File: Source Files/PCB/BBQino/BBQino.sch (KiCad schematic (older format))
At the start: 0 parts

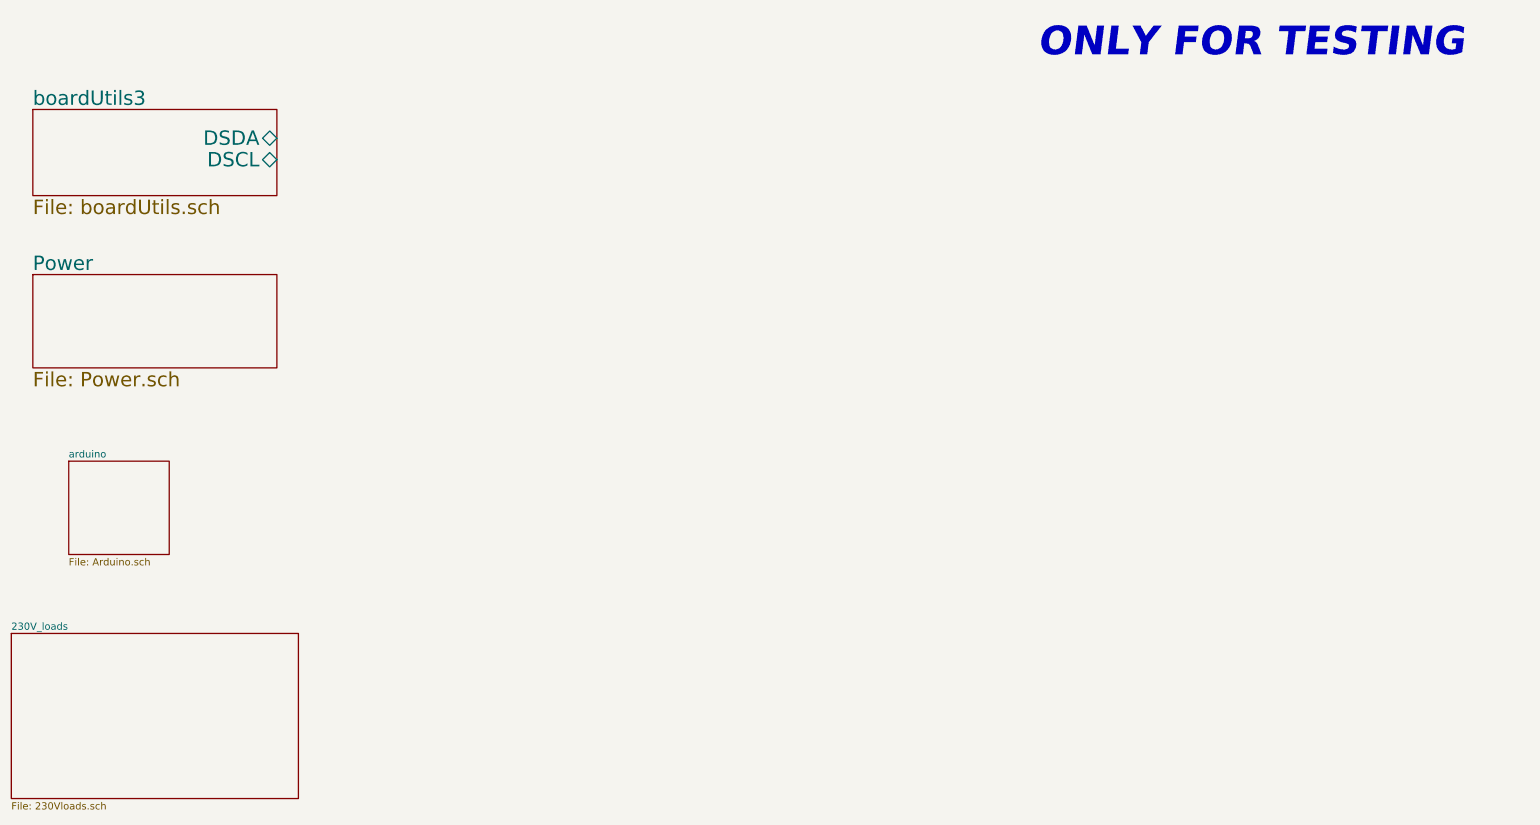
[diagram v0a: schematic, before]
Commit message: added thermocouple interface
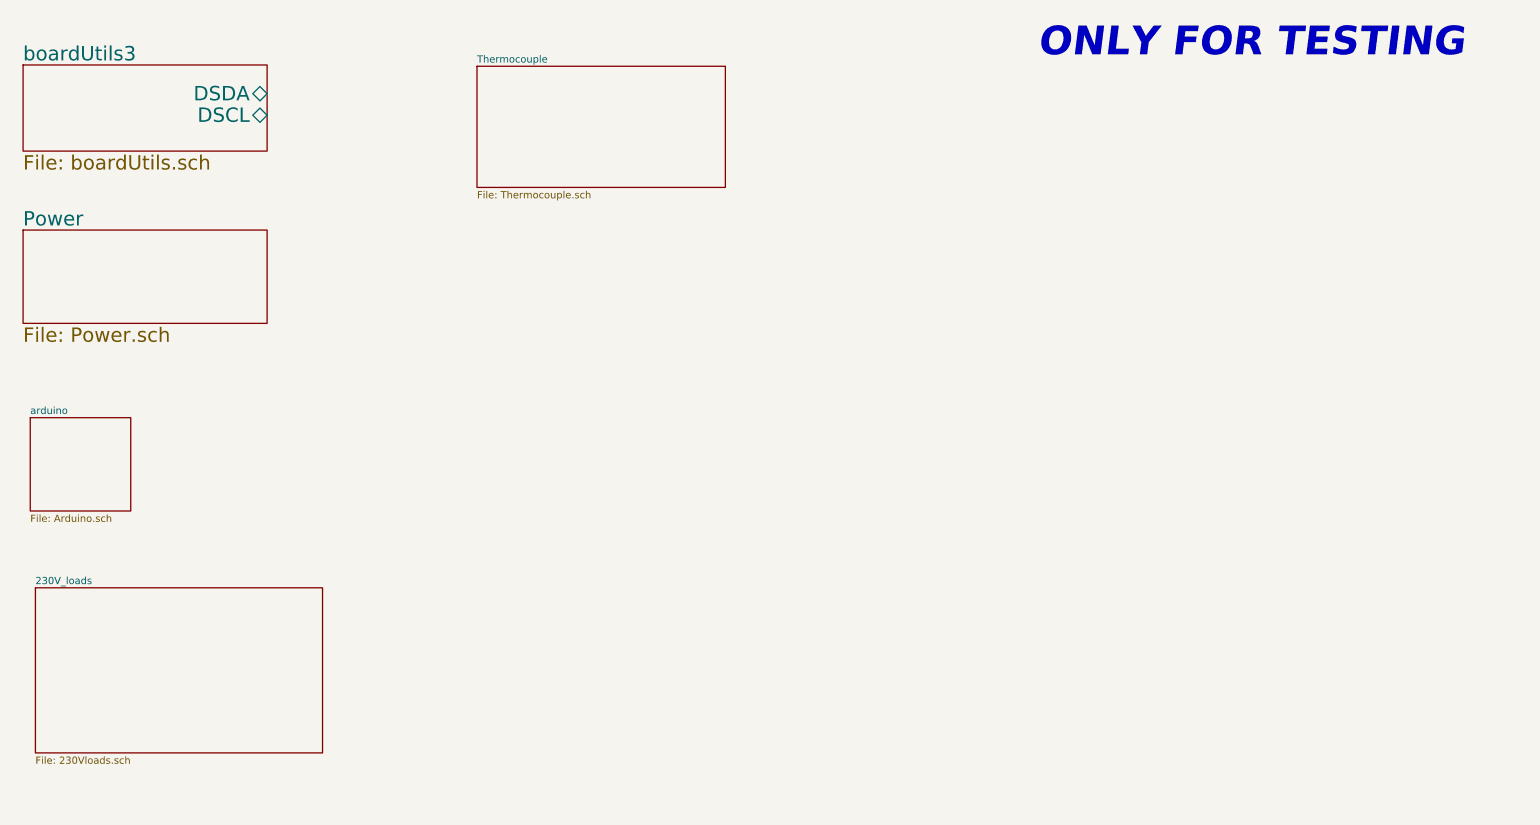
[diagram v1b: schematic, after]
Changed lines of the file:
@@
 $Descr A4 11693 8268
 encoding utf-8
-Sheet 1 5
+Sheet 1 6
 Title "BBQino - DRAFT"
 Date "2021-09-08"
@@
 ONLY FOR TESTING
 $Sheet
-S 1100 1350 1700 600
+S 1032 1040 1700 600
 U 61391ED2
 F0 "boardUtils3" 100
 F1 "boardUtils.sch" 100
-F2 "DSDA" B R 2800 1550 100
-F3 "DSCL" B R 2800 1700 100
+F2 "DSDA" B R 2732 1240 100
+F3 "DSCL" B R 2732 1390 100
 $EndSheet
 $Sheet
-S 1100 2500 1700 650
+S 1032 2190 1700 650
 U 613C1456
 F0 "Power" 100
@@
 $EndSheet
 $Sheet
-S 1350 3800 700  650
+S 1082 3497 700  650
 U 613FC6D4
 F0 "arduino" 50
@@
 $EndSheet
 $Sheet
-S 950  5000 2000 1150
+S 1118 4682 2000 1150
 U 614A5E16
 F0 "230V_loads" 50
 F1 "230Vloads.sch" 50
 $EndSheet
+$Sheet
+S 4194 1049 1730 844
+U 61534AF8
+F0 "Thermocouple" 50
+F1 "Thermocouple.sch" 50
+$EndSheet
 $EndSCHEMATC

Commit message: New architecture
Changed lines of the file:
@@
 $Descr A4 11693 8268
 encoding utf-8
-Sheet 1 6
+Sheet 1 7
 Title "BBQino - DRAFT"
 Date "2021-09-08"
@@
 F1 "Thermocouple.sch" 50
 $EndSheet
+$Sheet
+S 5100 2900 1300 800
+U 619F806C
+F0 "hbridge" 50
+F1 "hbridge.sch" 50
+$EndSheet
 $EndSCHEMATC
